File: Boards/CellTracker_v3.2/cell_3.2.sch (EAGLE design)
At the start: 30 parts, among them U2 LMR16020

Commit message: Finishing touches for Cell3.2
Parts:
- added X1: 53261-04, con-molex:53261-04
- C1: value (none) -> 0.3F
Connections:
- removed net IN_A: ISO7021.IN_A
- removed net N$12: R8.2, U$4.P$1
- removed net N$15: U$1.4/CAN-RX-PWM
- removed net N$16: U$1.5/PWM
- removed net N$33: U$1.6/PWM
- removed net OUT_B: ISO7021.OUT_B
- removed net VIN: C10.1, C9.1, R10.2, U$4.P$2, U2.VIN
- new net IN1: C10.1, C9.1, R10.2, U$4.P$1, U2.VIN
- new net N$11: R8.2, U$4.P$2
- new net NOTUSED: U$1.VIN
- new net RX_EX: ISO7021.OUT_A, X1-2.S
- new net TX_EX: ISO7021.IN_B, X1-3.S
- net +3V3: now also C3.1, ISO7021.VCC2; no longer C2.1, ISO7021.VCC1
- net GND: now also C3.2, ISO7021.GND2; no longer C2.2, ISO7021.GND1
- net GND_EX: now also C2.2, ISO7021.GND1, X1-4.S; no longer C3.2, ISO7021.GND2
- net IS_RX: now also ISO7021.OUT_B, U$1.9/RX2/PWM; no longer ISO7021.OUT_A
- net IS_TX: now also ISO7021.IN_A, U$1.10/TX2/PWM; no longer ISO7021.IN_B
- net N$2: now also U$1.16/A2/T; no longer U$1.14/A0
- net RX1: now also R2.2; no longer XB1.DOUT
- net RX3: now also XB1.DOUT; no longer R2.2
- net SD_CS: now also U$1.5/PWM; no longer U$1.10/TX2/PWM
- net SWITCH_LED: now also U$1.2; no longer U$1.3/CAN-TX/PWM
- net TX1: now also R6.2; no longer XB1.DIN/!CONFIG
- net TX3: now also XB1.DIN/!CONFIG; no longer R6.2
- net VCC_EX: now also C2.1, ISO7021.VCC1, X1-1.S; no longer C3.1, ISO7021.VCC2
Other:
- note added: "Conn"
- note added: "Digital Isolator"
- moved on the sheet: C10, C6, C7, C8, C9, D1, D2, ISO7021, L1, R1, R10, R2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

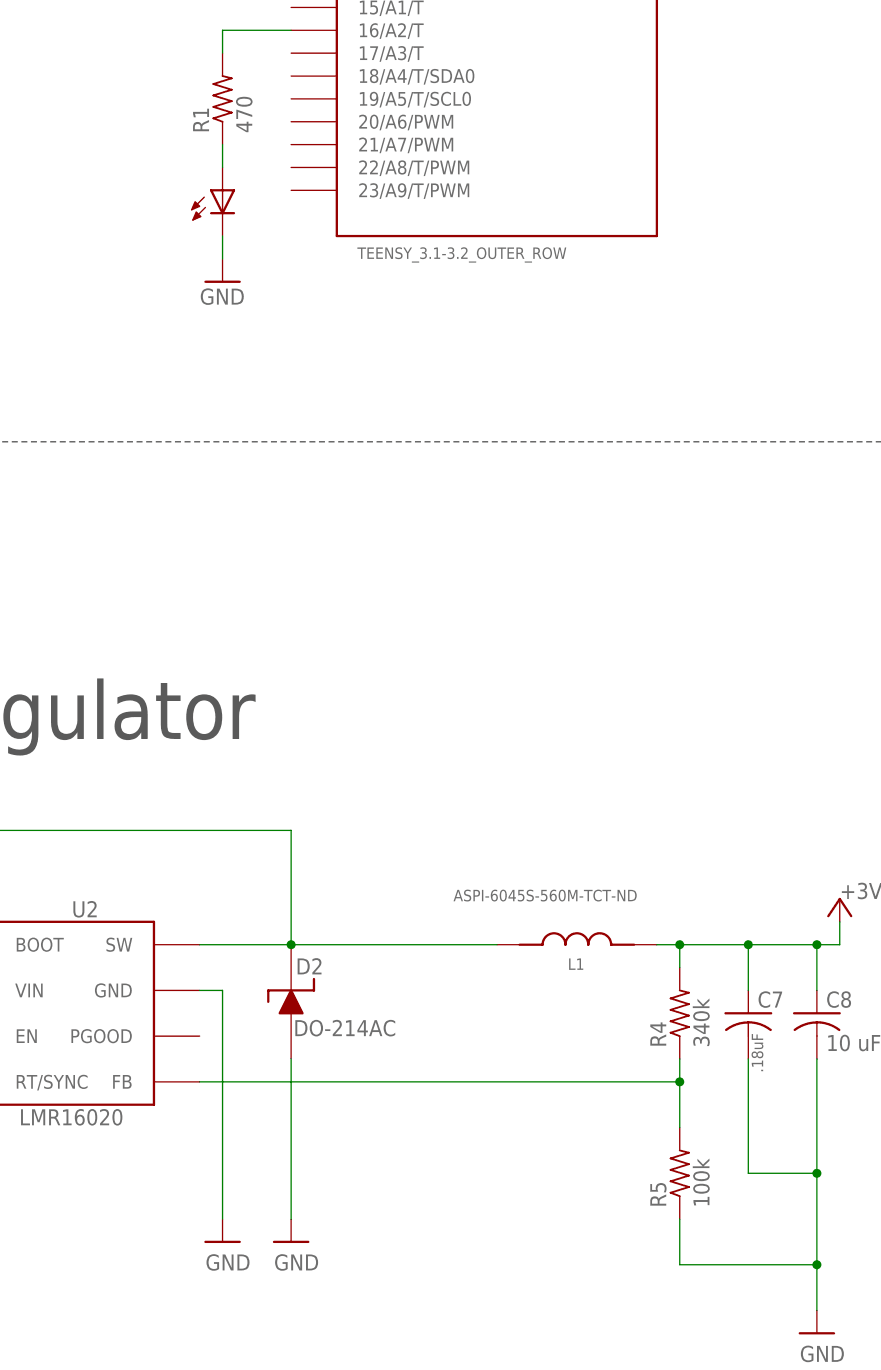
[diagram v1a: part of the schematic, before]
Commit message: Handling R values
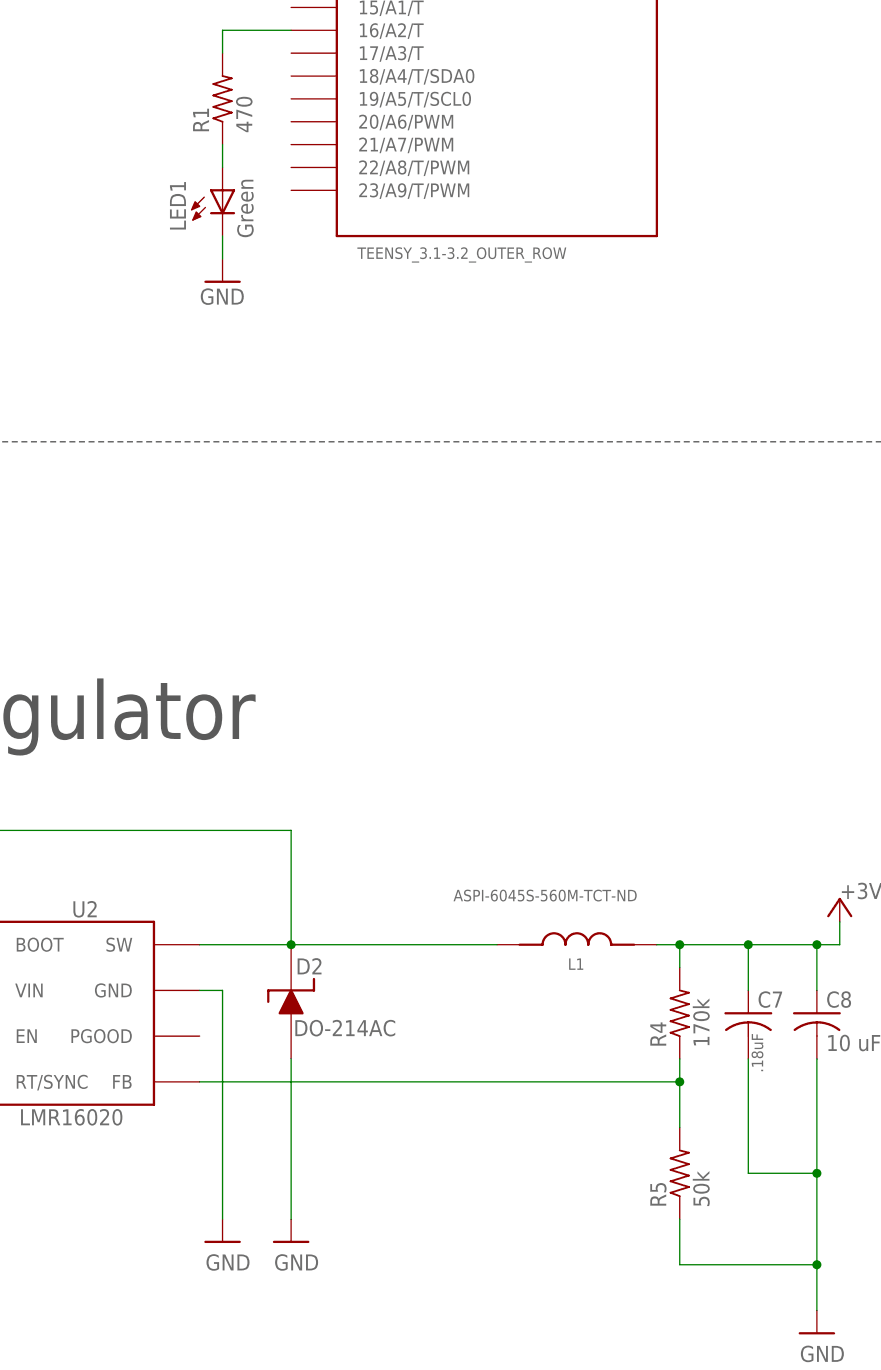
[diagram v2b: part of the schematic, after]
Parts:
- R4: value 340k -> 170k
- R5: value 100k -> 50k
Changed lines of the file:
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@@
 <part name="GND8" library="supply1" deviceset="GND" device=""/>
 <part name="R3" library="resistor" deviceset="R-US_" device="R0603" value="23.3k"/>
-<part name="R4" library="resistor" deviceset="R-US_" device="R0603" value="340k"/>
-<part name="R5" library="resistor" deviceset="R-US_" device="R0603" value="100k"/>
+<part name="R4" library="resistor" deviceset="R-US_" device="R0603" value="170k"/>
+<part name="R5" library="resistor" deviceset="R-US_" device="R0603" value="50k"/>
 <part name="C6" library="resistor" deviceset="C-US" device="C0805" value="0.1 uF"/>
 <part name="C9" library="resistor" deviceset="C-US" device="C1210" value="10 uF"/>
@@
 <attribute name="VALUE" x="54.61" y="234.442" size="1.778" layer="96"/>
 </instance>
-<instance part="LED1" gate="G$1" x="119.38" y="167.64" smashed="yes"/>
+<instance part="LED1" gate="G$1" x="119.38" y="167.64" smashed="yes">
+<attribute name="NAME" x="115.316" y="163.068" size="1.778" layer="95" rot="R90"/>
+<attribute name="VALUE" x="122.809" y="162.306" size="1.778" layer="96" rot="R90"/>
+</instance>
 <instance part="GND5" gate="1" x="119.38" y="157.48" smashed="yes">
 <attribute name="VALUE" x="116.84" y="154.94" size="1.778" layer="96"/>

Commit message: Cell Assem Fin
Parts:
- R4: value 170k -> 340k
- R5: value 50k -> 100k
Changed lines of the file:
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@@
 <part name="GND8" library="supply1" deviceset="GND" device=""/>
 <part name="R3" library="resistor" deviceset="R-US_" device="R0603" value="23.3k"/>
-<part name="R4" library="resistor" deviceset="R-US_" device="R0603" value="170k"/>
-<part name="R5" library="resistor" deviceset="R-US_" device="R0603" value="50k"/>
+<part name="R4" library="resistor" deviceset="R-US_" device="R0603" value="340k"/>
+<part name="R5" library="resistor" deviceset="R-US_" device="R0603" value="100k"/>
 <part name="C6" library="resistor" deviceset="C-US" device="C0805" value="0.1 uF"/>
 <part name="C9" library="resistor" deviceset="C-US" device="C1210" value="10 uF"/>
